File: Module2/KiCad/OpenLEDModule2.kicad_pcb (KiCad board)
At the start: 2 copper layers, 29.2 x 53.1 mm, 15 parts, among them P1 CONN2, P2 CONN1

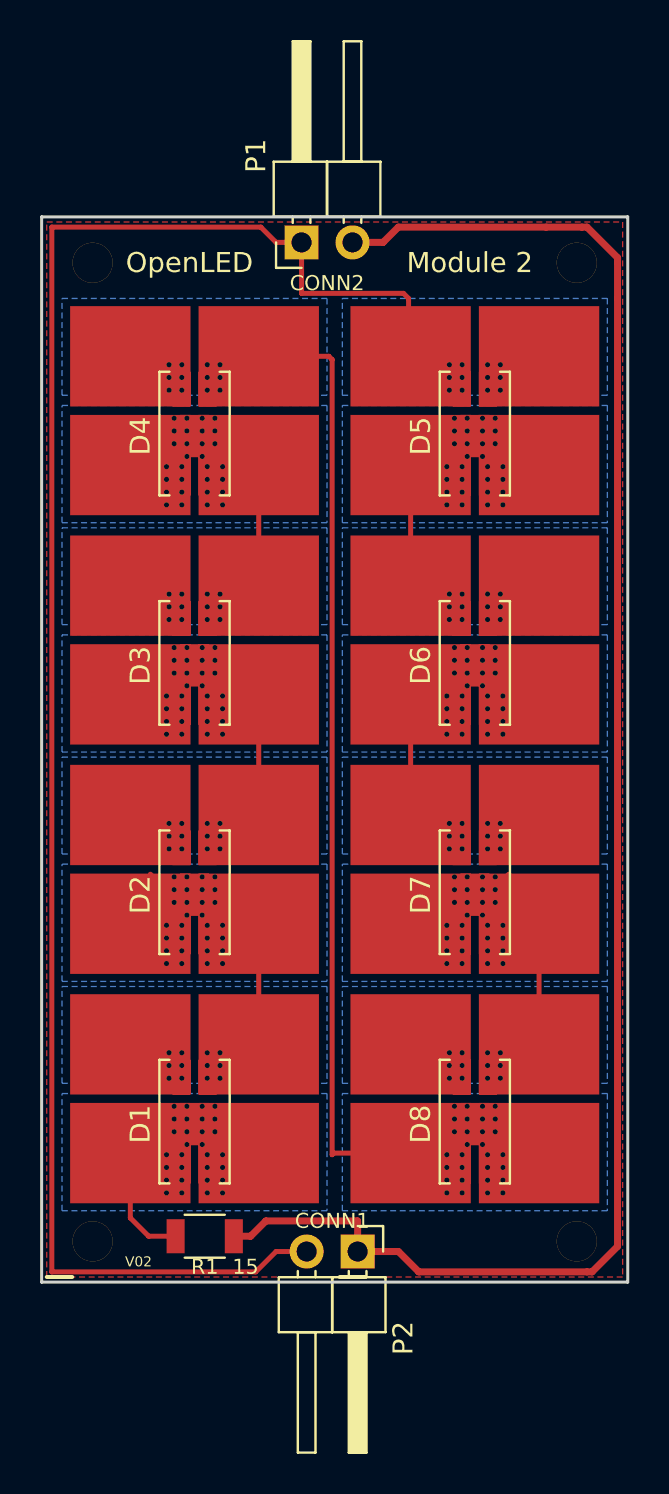
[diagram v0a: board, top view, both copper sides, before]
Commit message: Fixed issue #2 (header support)
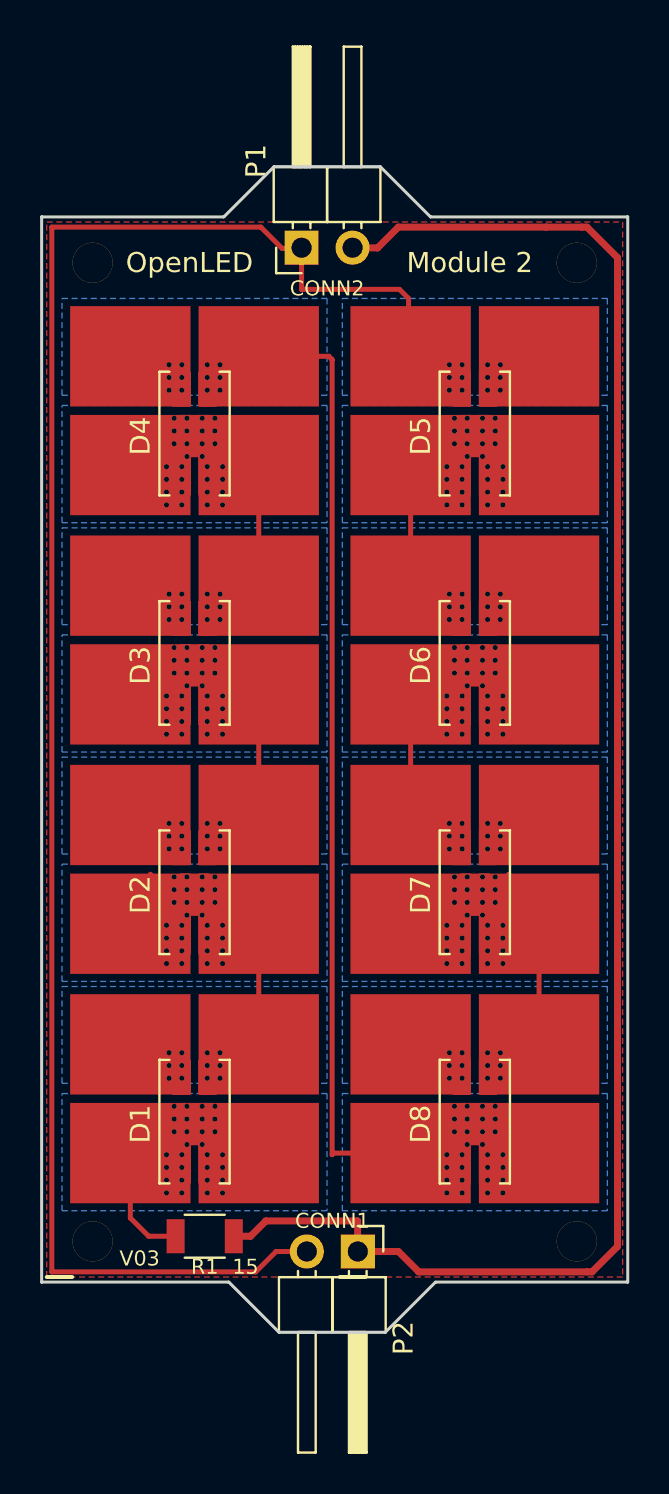
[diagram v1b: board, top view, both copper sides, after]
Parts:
- moved P1 0.27 mm to (142.8, 93.0)
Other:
- board size 29.2 x 53.1 mm -> 29.2 x 58.1 mm
- board text added: "V03"
- board text removed: "V02"
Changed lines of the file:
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@@
     (area 129.718999 82.234999 159.079001 153.477001)
     (thickness 1.6)
-    (drawings 9)
+    (drawings 17)
     (tracks 50)
     (zones 0)
@@
   )
   (module Pin_Headers:Pin_Header_Angled_1x02_Pitch2.54mm (layer F.Cu)
-    (at 142.748 92.71 90)
+    (at 142.75 92.975 90)
     (descr "Through hole angled pin header, 1x02, 2.54mm pitch, 6mm pin length, single row")
     (tags "Through hole angled pin header THT 1x02 2.54mm single row")
@@
   )
   (module Pin_Headers:Pin_Header_Angled_1x02_Pitch2.54mm (layer F.Cu)
-    (at 145.542 143.002 270)
+    (at 145.55 143 270)
     (descr "Through hole angled pin header, 1x02, 2.54mm pitch, 6mm pin length, single row")
     (tags "Through hole angled pin header THT 1x02 2.54mm single row")
@@
       (net 7 "Net-(D4-Pad1)"))
   )
-  (gr_text V02 (at 134.62 143.51) (layer F.SilkS)
-    (effects (font (size 0.5 0.5) (thickness 0.125)))
+  (gr_line (start 149.425 144.526) (end 159.004 144.526) (angle 90) (layer Edge.Cuts) (width 0.15))
+  (gr_line (start 141.625 147.026) (end 146.925 147.026) (angle 90) (layer Edge.Cuts) (width 0.15))
+  (gr_line (start 141.625 147.026) (end 139.125 144.526) (angle 90) (layer Edge.Cuts) (width 0.15))
+  (gr_line (start 146.925 147.026) (end 149.425 144.526) (angle 90) (layer Edge.Cuts) (width 0.15))
+  (gr_line (start 149.175 91.44) (end 159.004 91.44) (angle 90) (layer Edge.Cuts) (width 0.15))
+  (gr_line (start 141.375 88.94) (end 138.875 91.44) (angle 90) (layer Edge.Cuts) (width 0.15))
+  (gr_line (start 146.675 88.94) (end 141.375 88.94) (angle 90) (layer Edge.Cuts) (width 0.15))
+  (gr_line (start 146.675 88.94) (end 149.175 91.44) (angle 90) (layer Edge.Cuts) (width 0.15))
+  (gr_text V03 (at 134.675 143.35) (layer F.SilkS)
+    (effects (font (size 0.75 0.75) (thickness 0.125)))
   )
   (gr_text "Module 2" (at 151.13 93.726) (layer F.SilkS)
@@
   (gr_line (start 144.653 144.272) (end 145.923 144.272) (angle 90) (layer F.SilkS) (width 0.2))
   (gr_line (start 129.794 144.526) (end 129.794 91.44) (angle 90) (layer Edge.Cuts) (width 0.15))
-  (gr_line (start 159.004 144.526) (end 129.794 144.526) (angle 90) (layer Edge.Cuts) (width 0.15))
+  (gr_line (start 139.125 144.526) (end 129.794 144.526) (angle 90) (layer Edge.Cuts) (width 0.15))
   (gr_line (start 159.004 91.44) (end 159.004 144.526) (angle 90) (layer Edge.Cuts) (width 0.15))
-  (gr_line (start 129.794 91.44) (end 159.004 91.44) (angle 90) (layer Edge.Cuts) (width 0.15))
+  (gr_line (start 129.794 91.44) (end 138.875 91.44) (angle 90) (layer Edge.Cuts) (width 0.15))
   (segment (start 143.002 143.002) (end 141.478 143.002) (width 0.25) (layer F.Cu) (net 1))
-  (segment (start 141.478 92.71) (end 142.748 92.71) (width 0.25) (layer F.Cu) (net 1))
-  (segment (start 140.716 91.948) (end 141.478 92.71) (width 0.25) (layer F.Cu) (net 1))
+  (segment (start 141.778 93.01) (end 142.748 93.01) (width 0.25) (layer F.Cu) (net 1))
+  (segment (start 140.716 91.948) (end 141.778 93.01) (width 0.25) (layer F.Cu) (net 1))
   (segment (start 130.302 91.948) (end 140.716 91.948) (width 0.25) (layer F.Cu) (net 1))
   (segment (start 130.302 144.018) (end 130.302 91.948) (width 0.25) (layer F.Cu) (net 1))
   (segment (start 140.462 144.018) (end 130.302 144.018) (width 0.25) (layer F.Cu) (net 1))
   (segment (start 141.478 143.002) (end 140.462 144.018) (width 0.25) (layer F.Cu) (net 1))
-  (segment (start 142.748 92.71) (end 142.748 95.25) (width 0.25) (layer F.Cu) (net 1))
+  (segment (start 142.748 93.01) (end 142.748 95.05) (width 0.25) (layer F.Cu) (net 1))
   (segment (start 148.082 95.504) (end 148.082 98.285) (width 0.25) (layer F.Cu) (net 1))
-  (segment (start 147.828 95.25) (end 148.082 95.504) (width 0.25) (layer F.Cu) (net 1))
-  (segment (start 142.748 95.25) (end 147.828 95.25) (width 0.25) (layer F.Cu) (net 1))
+  (segment (start 147.628 95.05) (end 148.082 95.504) (width 0.25) (layer F.Cu) (net 1))
+  (segment (start 142.748 95.05) (end 147.628 95.05) (width 0.25) (layer F.Cu) (net 1))
   (segment (start 148.082 98.285) (end 148.184 98.387) (width 0.25) (layer F.Cu) (net 1))
   (segment (start 136.472 142.24) (end 135.128 142.24) (width 0.25) (layer F.Cu) (net 2))
@@
   (segment (start 156.718 91.948) (end 154.94 91.948) (width 0.35) (layer F.Cu) (net 3))
   (segment (start 154.94 91.948) (end 147.574 91.948) (width 0.35) (layer F.Cu) (net 3))
-  (segment (start 147.574 91.948) (end 146.812 92.71) (width 0.35) (layer F.Cu) (net 3))
-  (segment (start 146.812 92.71) (end 145.288 92.71) (width 0.35) (layer F.Cu) (net 3))
+  (segment (start 147.574 91.948) (end 146.537 92.985) (width 0.35) (layer F.Cu) (net 3))
+  (segment (start 146.537 92.985) (end 145.413 92.985) (width 0.35) (layer F.Cu) (net 3))
   (segment (start 156.972 144.018) (end 157.226 144.018) (width 0.35) (layer F.Cu) (net 3))
   (segment (start 157.226 144.018) (end 158.496 142.748) (width 0.35) (layer F.Cu) (net 3))
